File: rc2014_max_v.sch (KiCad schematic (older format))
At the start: 34 parts, among them J1 M3 Mounting Hole, J2 Conn_01x40, J3 Conn_01x24, U1 TXB0108PWR, U2 TXB0108PWR, U3 TXB0108PWR, U4 TXB0108PWR, U5 TXB0108PWR, U6 TXB0108PWR, U7 TXB0108PWR

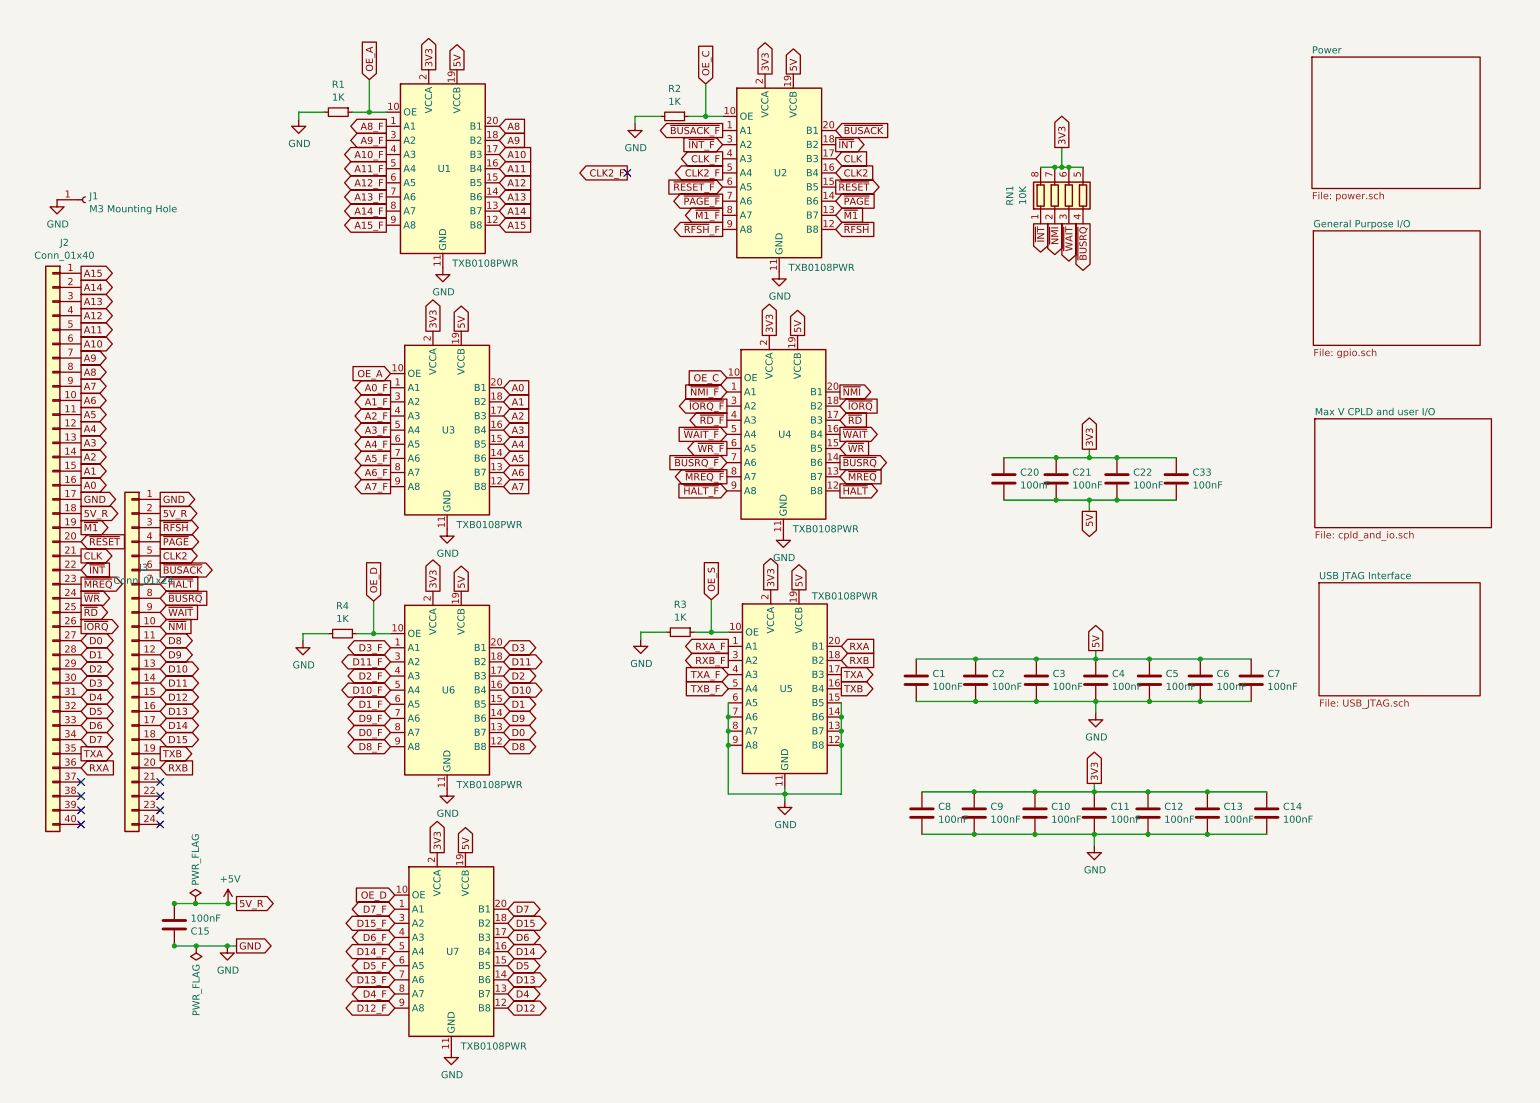
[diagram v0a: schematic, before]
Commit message: replaced some global pins with hierarchical sheet pins
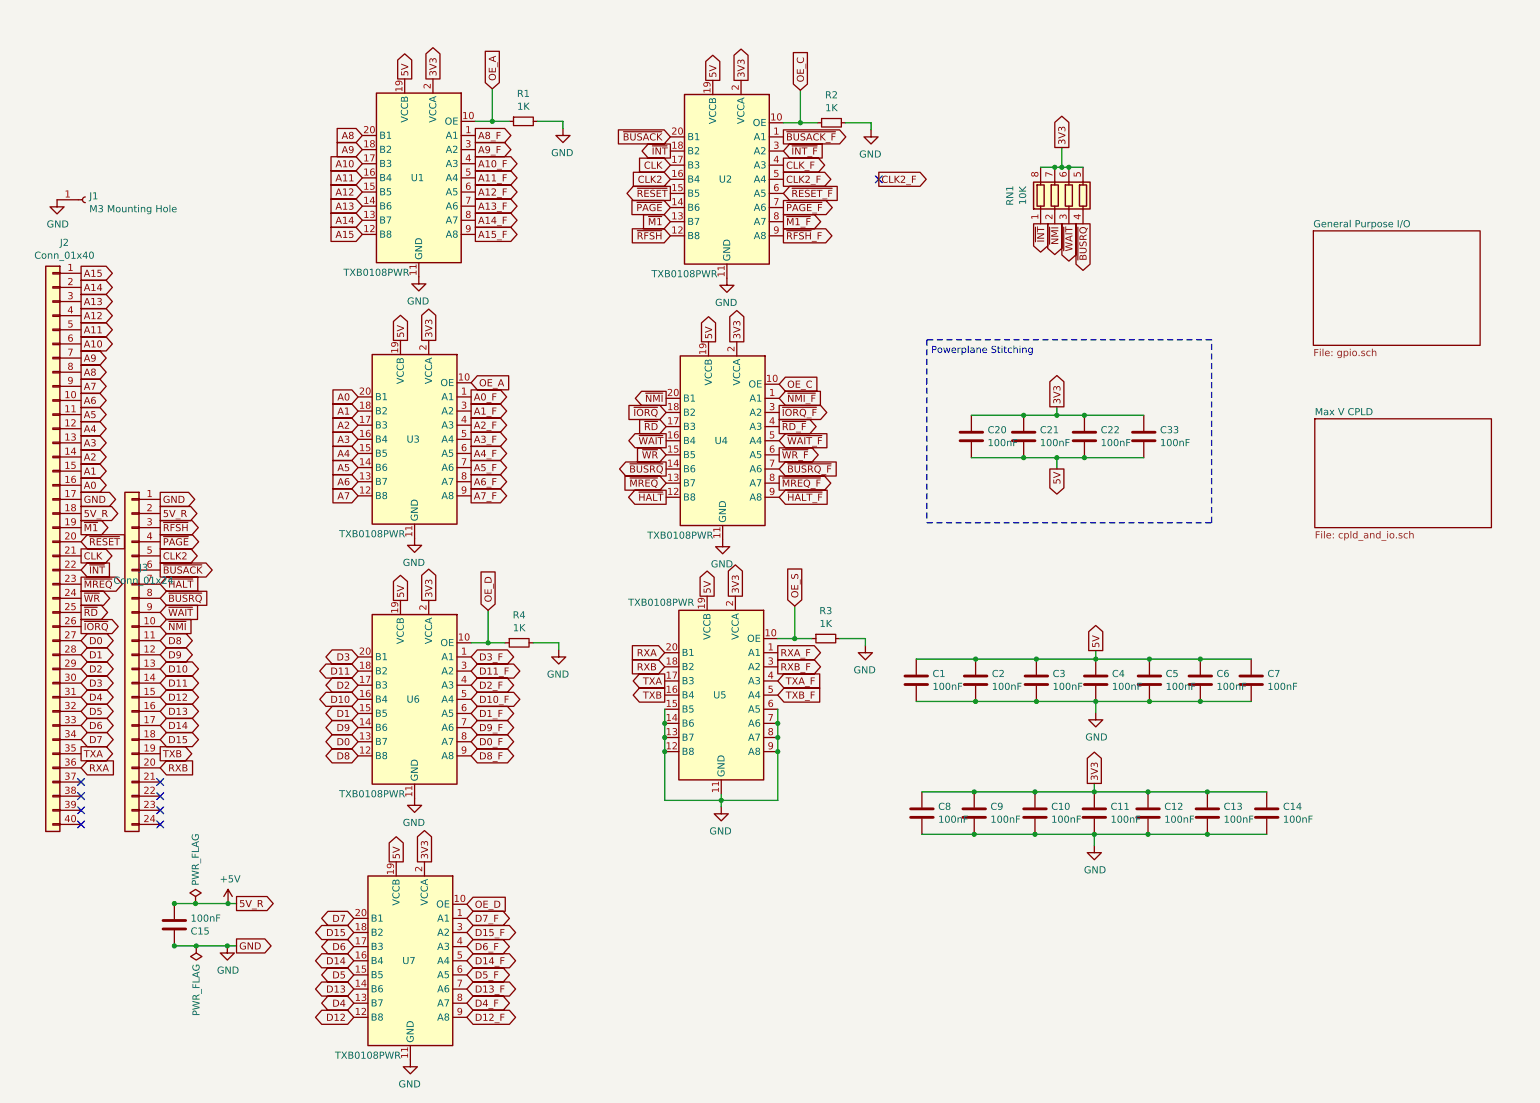
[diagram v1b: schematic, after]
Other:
- note added: "Powerplane Stitching"
- moved on the sheet: C20, C21, C22, C33, R1, R2, R3, R4, U1, U2, U3, U4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

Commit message: recovered layout
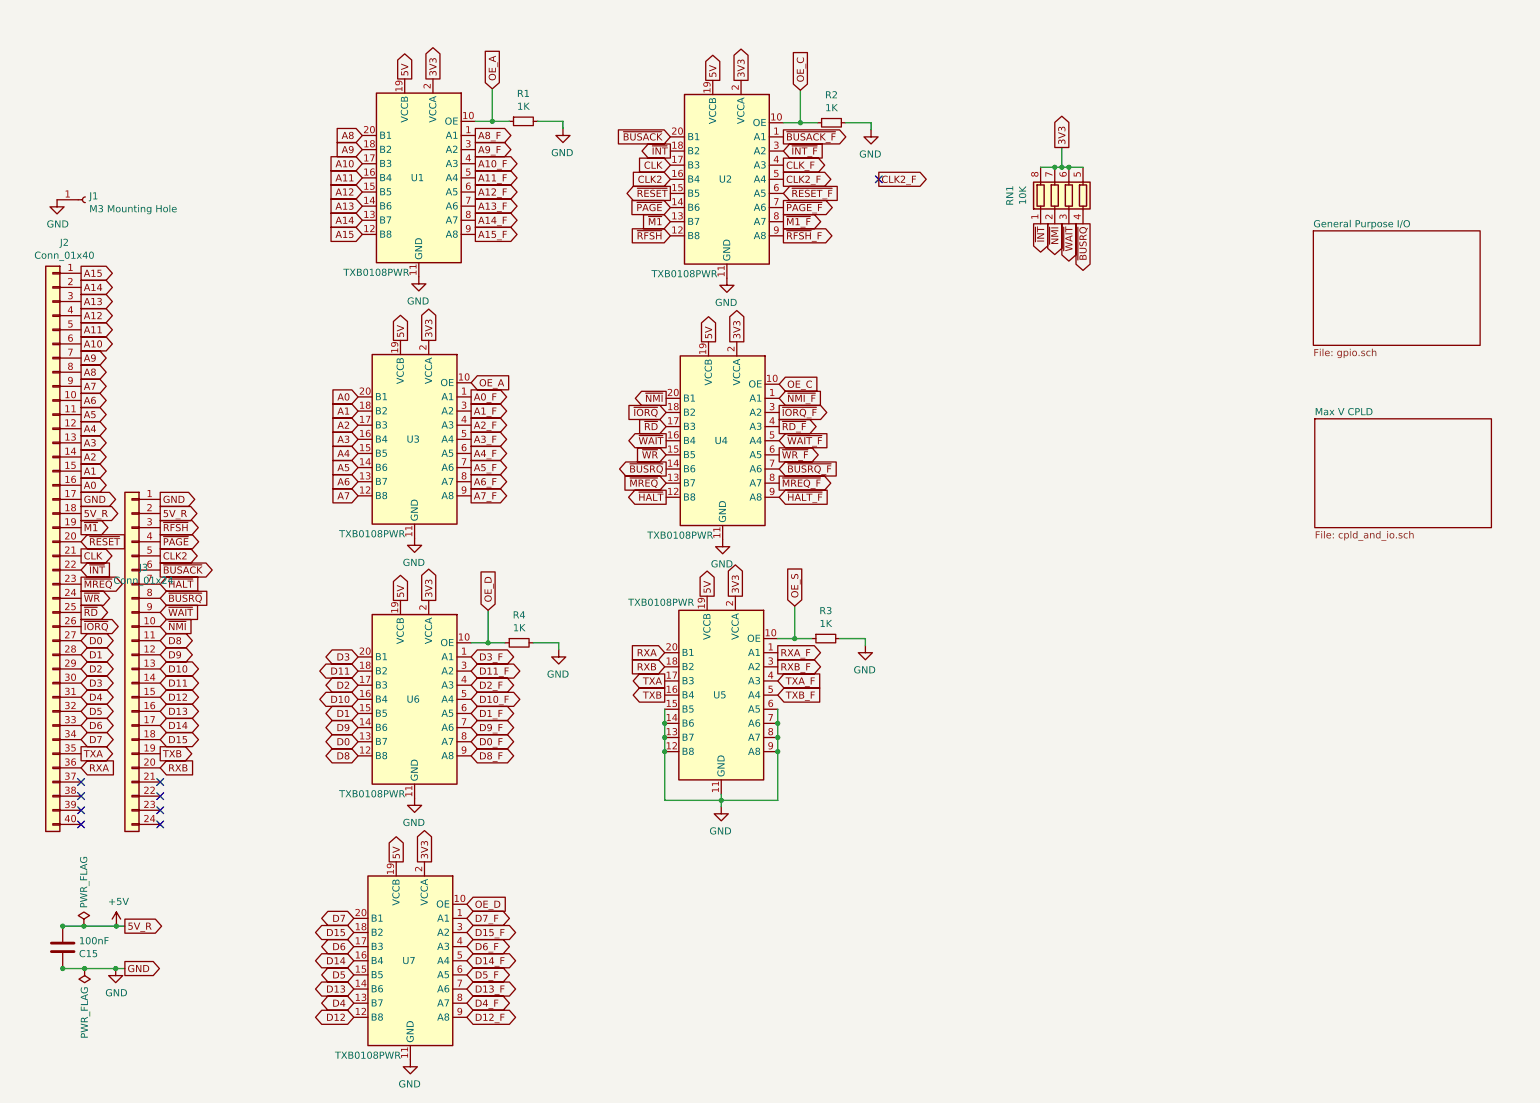
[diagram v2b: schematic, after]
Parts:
- removed C1, C10, C11, C12, C13, C14, C2, C3, C4, C5, C6, C7, C8, C9: 100nF, Capacitor_SMD:C_0603_1608Metric_Pad1.05x0.95mm_HandSolder, symbol Device:C
- removed C20, C21, C22, C33: 100nF, Capacitor_SMD:C_0805_2012Metric_Pad1.15x1.40mm_HandSolder, symbol Device:C
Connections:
- wire segments 83 -> 45
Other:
- note removed: "Powerplane Stitching"
- moved on the sheet: C15

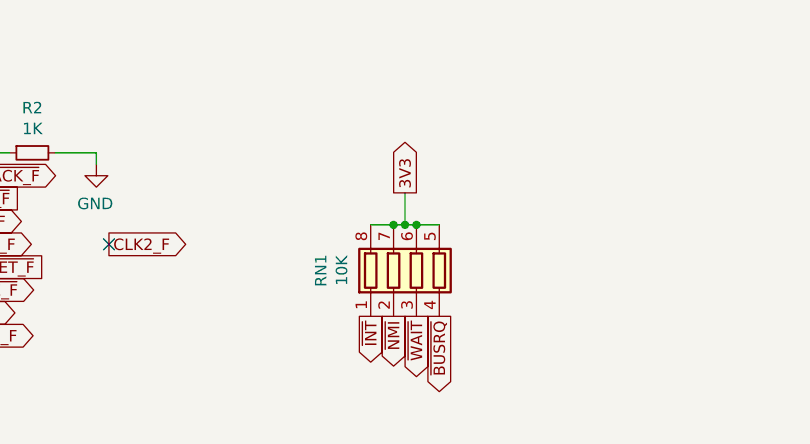
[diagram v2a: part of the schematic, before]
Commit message: placed all parts
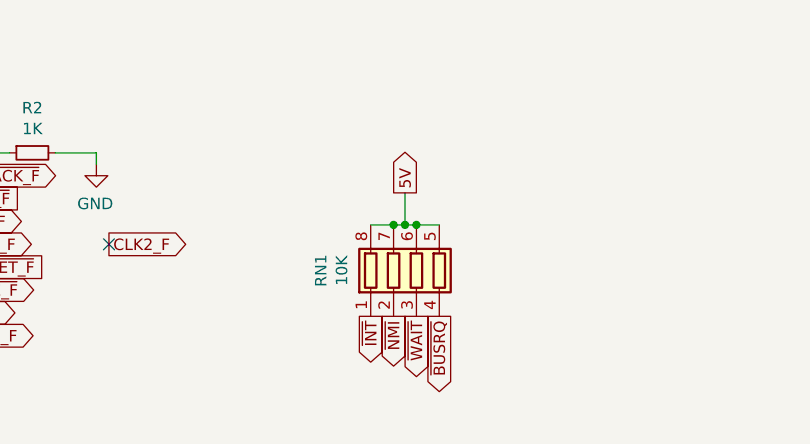
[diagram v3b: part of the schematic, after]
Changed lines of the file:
@@
 Text GLabel 5340 775  1    50   Output ~ 0
 5V
-Text GLabel 7810 1250 1    50   Output ~ 0
-3V3
 Wire Wire Line
 	730  7060 740  7060
@@
 	1    0    0    1
 $EndComp
+Text GLabel 7810 1250 1    50   Output ~ 0
+5V
 $EndSCHEMATC

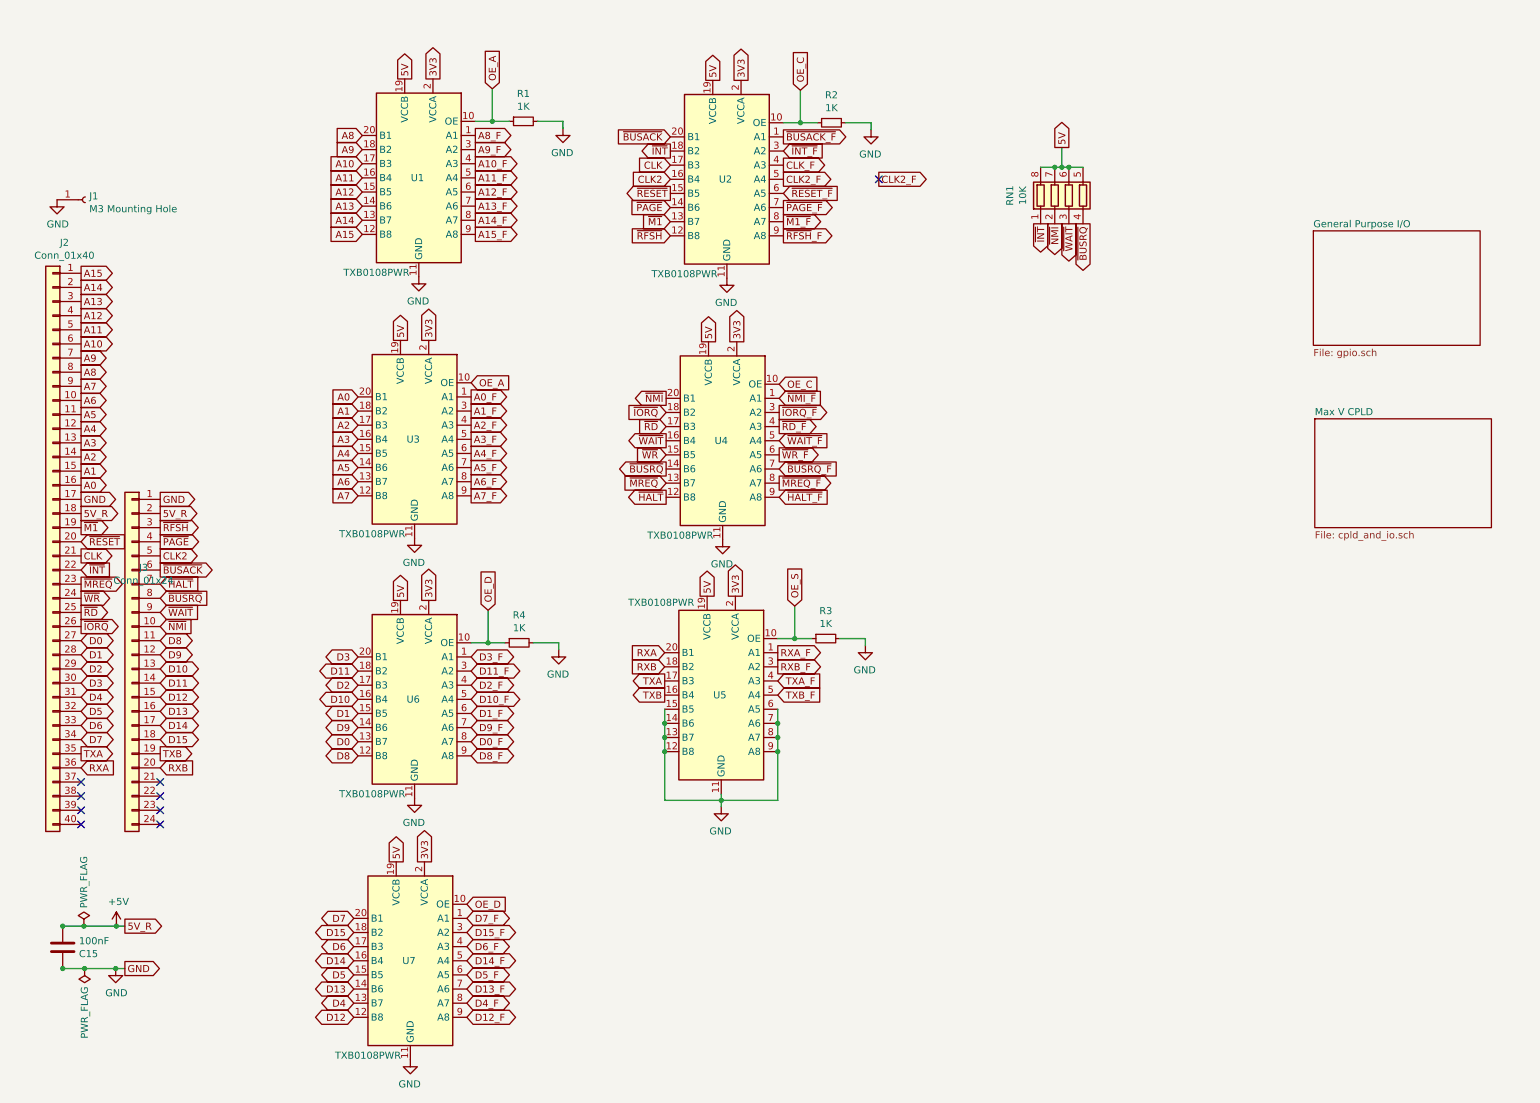
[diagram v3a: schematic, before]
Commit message: Added bus structure, additional pins added, 5V load balancer
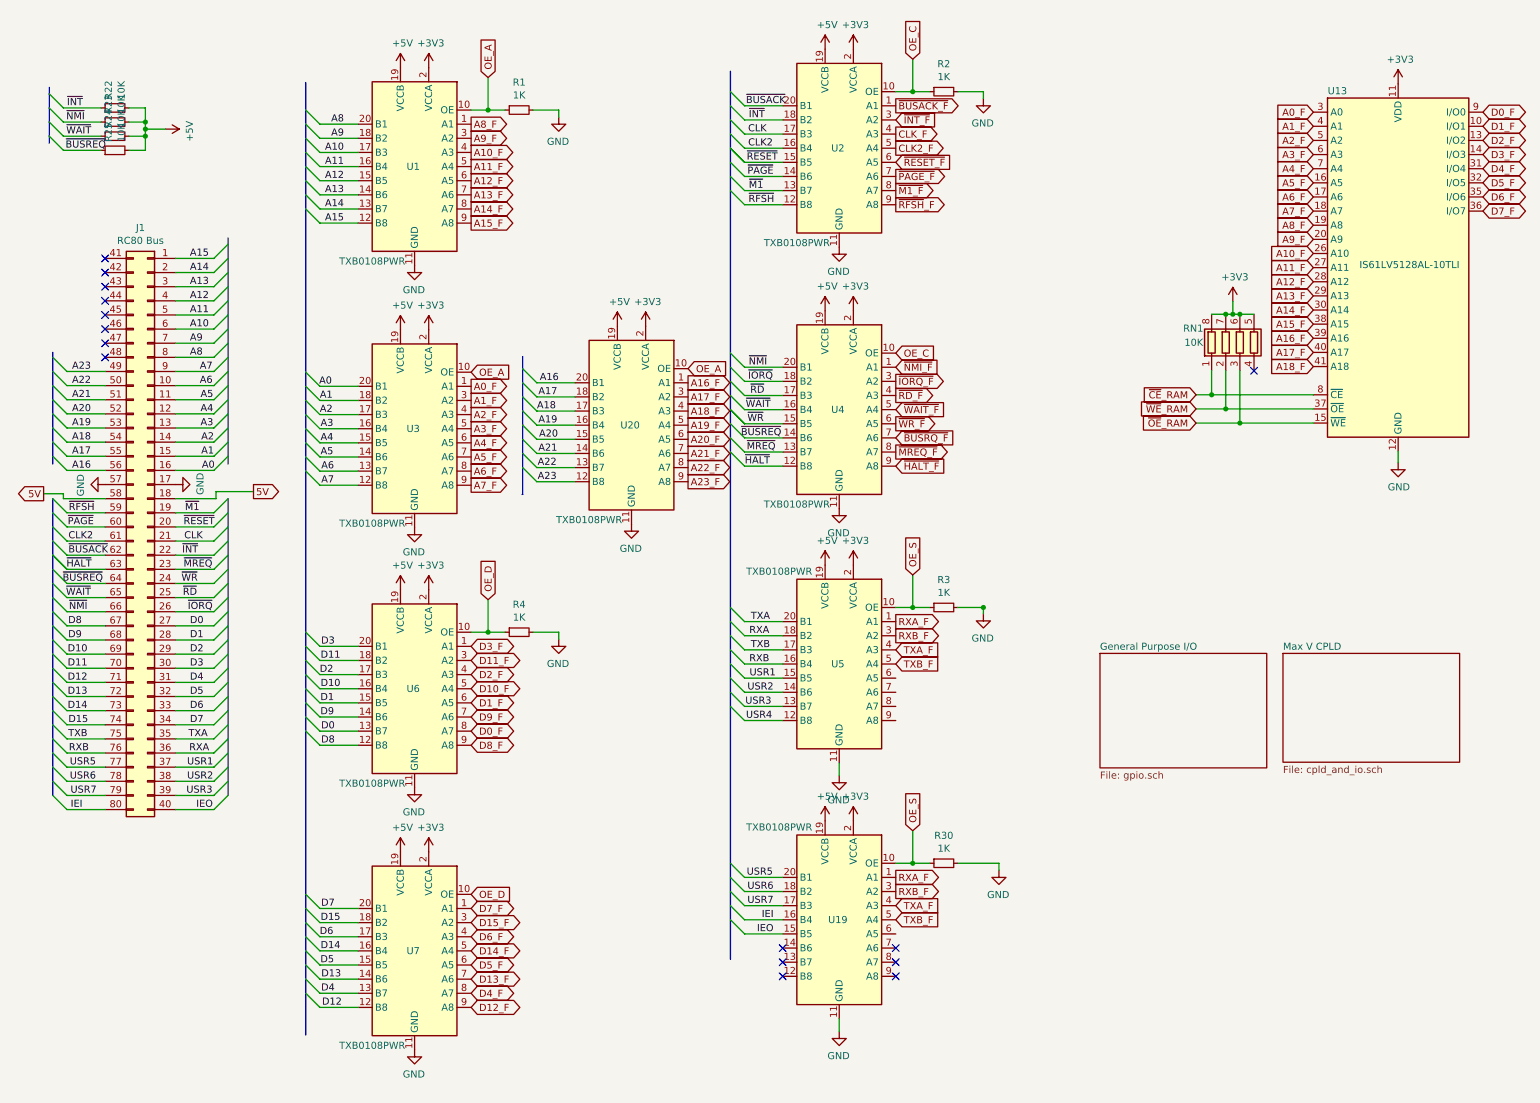
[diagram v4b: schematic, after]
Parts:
- removed C15: 100nF, Capacitor_SMD:C_0603_1608Metric_Pad1.05x0.95mm_HandSolder, symbol Device:C
- removed J1: M3 Mounting Hole, MountingHole:MountingHole_3.2mm_M3_ISO14580_Pad, symbol Connector:Conn_01x01_Female
- removed J2: Conn_01x40, Connector_PinHeader_2.54mm:PinHeader_1x40_P2.54mm_Horizontal, symbol Connector_Generic:Conn_01x40
- removed J3: Conn_01x24, Connector_PinHeader_2.54mm:PinHeader_1x24_P2.54mm_Vertical, symbol Connector_Generic:Conn_01x24
- added J1: RC80 Bus, Connector_PinHeader_2.54mm:PinHeader_2x40_Top_Bottom_P2.54mm_Horizontal, symbol Connector_Generic:Conn_02x40_Top_Bottom
- added R22, R23, R24, R25: 10K, Resistor_SMD:R_0603_1608Metric_Pad1.05x0.95mm_HandSolder, symbol Device:R_Small
- added R30: 1K, Resistor_SMD:R_0603_1608Metric_Pad1.05x0.95mm_HandSolder, symbol Device:R_Small
- added U13: IS61LV5128AL-10TLI, Package_SO:TSOP-II-44_10.16x18.41mm_P0.8mm, symbol rc2014_max_v-rescue:IS61LV5128AL-10TLI-Memory_RAM
- added U19, U20: TXB0108PWR, Package_SO:TSSOP-20_4.4x6.5mm_P0.65mm, symbol rc2014_max_v-rescue:TXB0108PWR-Logic_LevelTranslator
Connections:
- net labels added: +3V3, A16, A16_F, A17, A17_F, A18, A18_F, A19, A19_F, A20, A20_F, A21, A21_F, A22, A22_F, A23, A23_F, IEI, IEO, USR1, USR2, USR3, USR4, USR5, USR6, USR7, ~BUSREQ, ~CE~_RAM, ~OE~_RAM, ~WE~_RAM
- net labels removed: 3V3, 5V_R, ~BUSRQ
- wire segments 45 -> 199
- no-connect marks 9 -> 15
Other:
- moved on the sheet: R1, R2, R3, R4, U1, U2, U3, U4, U5, U6, U7
